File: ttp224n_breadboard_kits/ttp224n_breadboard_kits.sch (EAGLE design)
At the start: 20 parts, among them U1 TTP224N-BSB

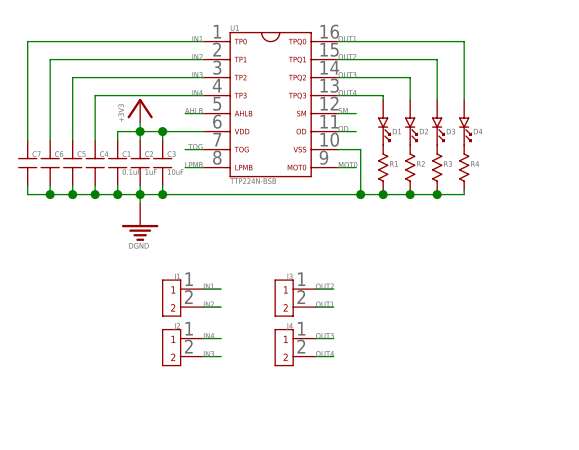
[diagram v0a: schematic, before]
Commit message: the ttp224n breadboard kits is done
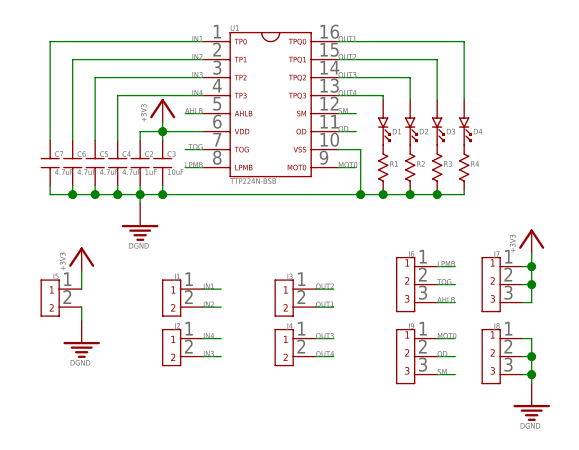
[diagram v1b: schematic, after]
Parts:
- removed C1: 0.1uF, Capacitors:CAPACITOR_FIXED_0805
- added J5: (no value), Connectors:2PIN_HEADER_PITCH2.54MM_TH
- added J6, J7, J8, J9: (no value), Connectors:3PIN_HEADER_PITCH2.54MM_TH
- C4, C5, C6, C7: value (none) -> 4.7uF
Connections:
- net +3V3: now also J5.1, J7.1, J7.2, J7.3; no longer C1.1
- net AHLB: now also J6.3
- net DGND: now also J5.2, J8.1, J8.2, J8.3; no longer C1.2
- net LPMB: now also J6.1
- net MOT0: now also J9.1
- net OD: now also J9.2
- net SM: now also J9.3
- net TOG: now also J6.2
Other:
- moved on the sheet: C4, C5, C6, C7

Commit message: update the ttp224 touchpad module
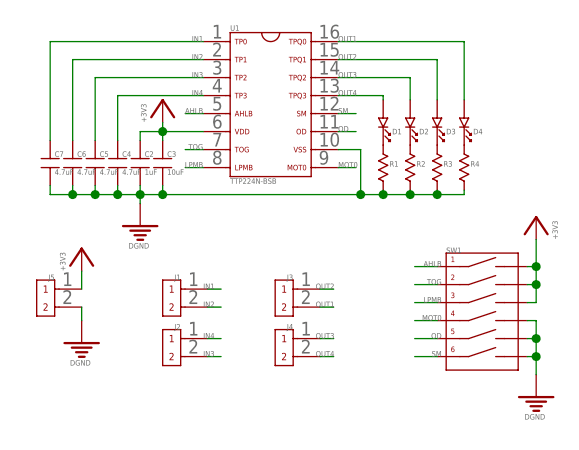
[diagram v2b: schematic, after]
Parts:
- removed J6, J7, J8, J9: (no value), Connectors:3PIN_HEADER_PITCH2.54MM_TH
- added SW1: (no value), Switches:DIP_SWITCH_6PIN-219-6MST
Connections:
- net +3V3: now also SW1.1.1, SW1.2.1, SW1.3.1; no longer J7.1, J7.2, J7.3
- net AHLB: now also SW1.1.0; no longer J6.3
- net DGND: now also SW1.4.1, SW1.5.1, SW1.6.1; no longer J8.1, J8.2, J8.3
- net LPMB: now also SW1.3.0; no longer J6.1
- net MOT0: now also SW1.4.0; no longer J9.1
- net N$1: now also D1.K; no longer D1.1
- net N$3: now also D2.K; no longer D2.1
- net N$4: now also D3.K; no longer D3.1
- net N$5: now also D4.K; no longer D4.1
- net OD: now also SW1.5.0; no longer J9.2
- net OUT1: now also D4.A; no longer D4.2
- net OUT2: now also D3.A; no longer D3.2
- net OUT3: now also D2.A; no longer D2.2
- net OUT4: now also D1.A; no longer D1.2
- net SM: now also SW1.6.0; no longer J9.3
- net TOG: now also SW1.2.0; no longer J6.2
